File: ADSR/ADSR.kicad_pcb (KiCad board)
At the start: 2 copper layers, 44.7 x 104.3 mm, 45 parts, among them J1 Panel, J2 Power, Q1 BC547, Q2 BC547, Q3 BC547, U1 LM358, U2 ICM7555

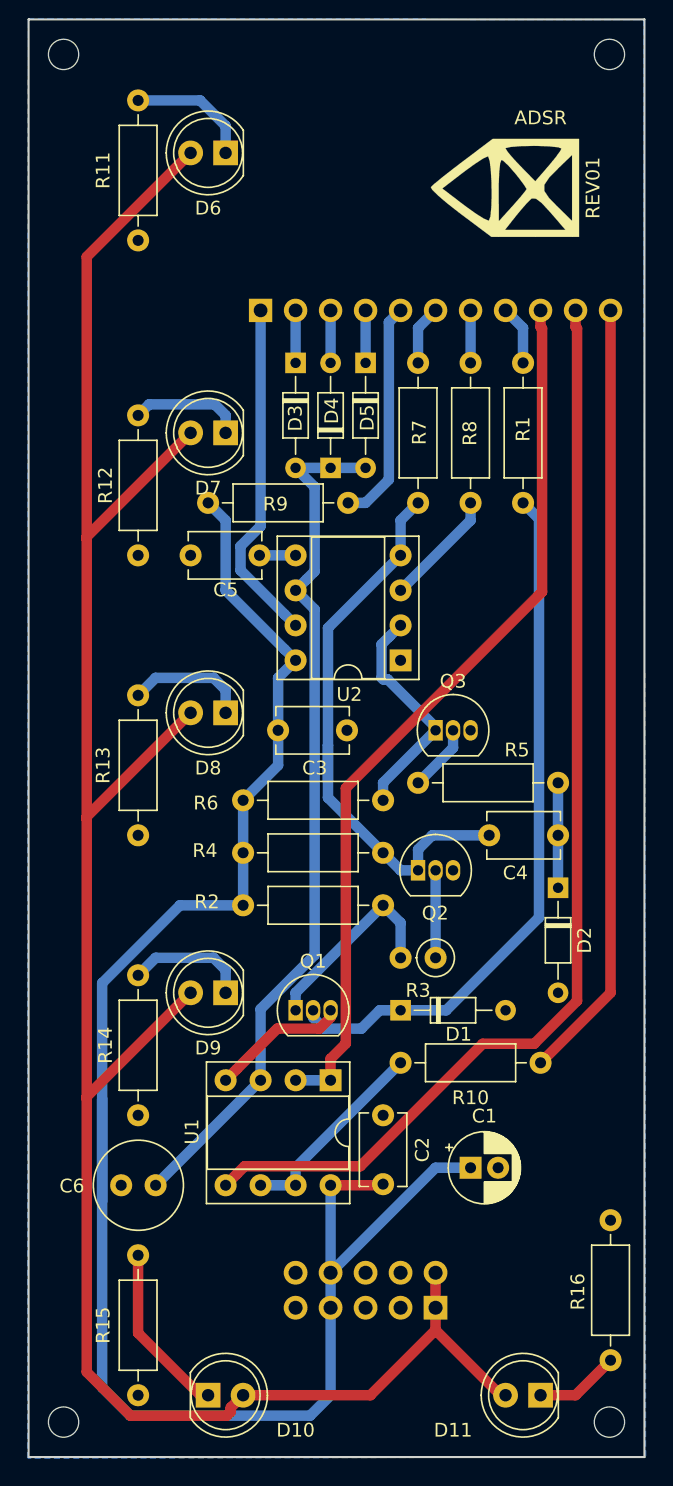
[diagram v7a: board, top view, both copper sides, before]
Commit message: finalizy modules: ADSR, Bass++ and VCO1
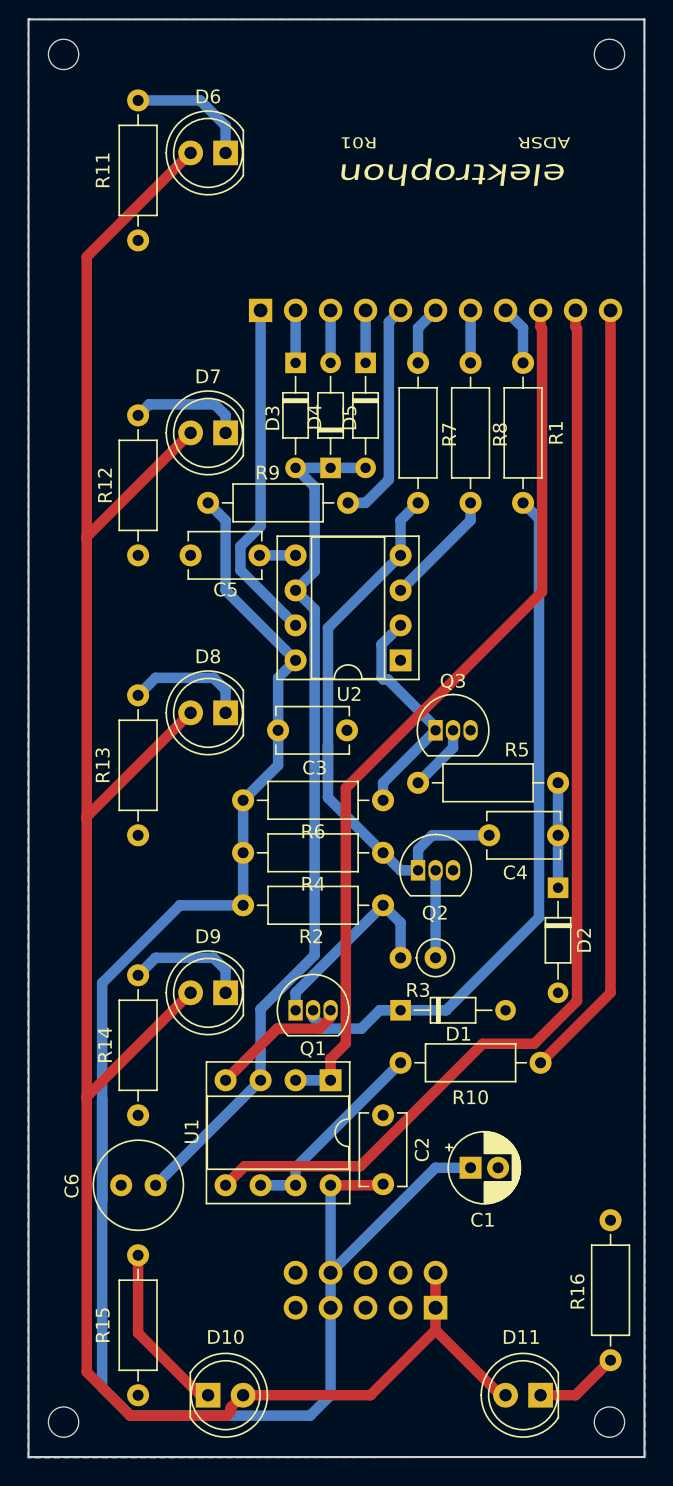
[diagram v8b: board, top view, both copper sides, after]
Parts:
- removed G***: LOGO, logo:spielhuus
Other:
- board text added: "+15V"
- board text added: "-15V"
- board text added: "1"
- board text added: "10"
- board text added: "11"
- board text added: "2"
- board text added: "3"
- board text added: "4"
- board text added: "5"
- board text added: "5V"
- board text added: "6"
- board text added: "7"
- board text added: "8"
- board text added: "9"
- board text added: "GND"
- board text added: "R01"
- board text added: "elektrophon"
- board text removed: "REV01"
